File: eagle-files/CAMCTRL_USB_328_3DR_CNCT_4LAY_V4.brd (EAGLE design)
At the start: 56.6 x 37.5 mm, 71 parts, among them IC2 lm1117, J1 ICSP, Q1 12MHz, U1 M3421E, U2 ATMEGA168, U3 3.3V_REG, U4 TS3USB30EDGSR, Y1 16MHz

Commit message: Updated Code and Board
Updated test code with new object info handling, zooming command and
some extra clean-ups.
Board updated with replaced LED's resistors.
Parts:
- R13, R2, R6: value 1K -> 220R
- R14: value 330 -> 100R
- R17, R18: value 270R -> 220R
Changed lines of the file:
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@@
 </element>
 <element name="Q1" library="SparkFun-FreqCtrl" package="CRYSTAL-SMD-5X3" value="12MHz" x="11.43" y="12.065" rot="R90"/>
-<element name="R2" library="pel_dipol_comp" package="0402-RES" value="1K" x="35.56" y="8.255" rot="R90"/>
+<element name="R2" library="pel_dipol_comp" package="0402-RES" value="220R" x="35.56" y="8.255" rot="R90"/>
 <element name="C2" library="pel_dipol_comp" package="0402-CAP" value="0.1uF" x="41.91" y="6.35" rot="R270"/>
 <element name="LED1" library="pel_dipol_comp" package="0603-LED" value="GREEN" x="35.56" y="11.43" smashed="yes" rot="R270">
@@
 <attribute name="VALUE" x="37.084" y="10.3505" size="0.4064" layer="27"/>
 </element>
-<element name="R14" library="pel_dipol_comp" package="0402-RES" value="330" x="38.1" y="8.255" rot="R90"/>
+<element name="R14" library="pel_dipol_comp" package="0402-RES" value="100R" x="38.1" y="8.255" rot="R90"/>
 <element name="C10" library="SparkFun" package="EIA3216" value="10uF" x="6.985" y="3.175" rot="R270"/>
 <element name="F1" library="SparkFun" package="PTC-1206" value="PTCSMD" x="10.16" y="21.336"/>
@@
 <attribute name="VALUE" x="18.923" y="18.161" size="0.4064" layer="27" font="vector" rot="R90"/>
 </element>
-<element name="R6" library="pel_dipol_comp" package="0402-RES" value="1K" x="33.02" y="8.255" rot="R90"/>
+<element name="R6" library="pel_dipol_comp" package="0402-RES" value="220R" x="33.02" y="8.255" rot="R90"/>
 <element name="LED3" library="pel_dipol_comp" package="0603-LED" value="BLUE" x="33.02" y="11.43" smashed="yes" rot="R270">
 <attribute name="NAME" x="32.3215" y="9.271" size="0.635" layer="25" ratio="16" rot="R90"/>
@@
 <element name="SJ1" library="SparkFun-Passives" package="SJ_3_PASTE2&amp;3" value="" x="35.56" y="27.94" rot="MR180"/>
 <element name="SJ2" library="SparkFun-Passives" package="SJ_2S-NO" value="SOLDERJUMPER-OLDNO" x="38.735" y="27.94" rot="MR180"/>
-<element name="R13" library="pel_dipol_comp" package="0402-RES" value="1K" x="40.64" y="8.255" rot="R90"/>
+<element name="R13" library="pel_dipol_comp" package="0402-RES" value="220R" x="40.64" y="8.255" rot="R90"/>
 <element name="LED4" library="pel_dipol_comp" package="0603-LED" value="BLUE" x="40.64" y="11.43" smashed="yes" rot="R270">
 <attribute name="NAME" x="39.9415" y="9.271" size="0.635" layer="25" ratio="16" rot="R90"/>
@@
 <attribute name="VALUE" x="46.7614" y="26.797" size="0.635" layer="27" font="vector" ratio="16" rot="R90"/>
 </element>
-<element name="R17" library="pel_dipol_comp" package="0402-RES" value="270R" x="45.085" y="22.86" smashed="yes" rot="R270">
+<element name="R17" library="pel_dipol_comp" package="0402-RES" value="220R" x="45.085" y="22.86" smashed="yes" rot="R270">
 <attribute name="NAME" x="45.9232" y="24.003" size="0.4064" layer="25" font="vector" ratio="16" rot="R270"/>
 <attribute name="VALUE" x="43.7896" y="24.003" size="0.635" layer="27" font="vector" ratio="16" rot="R270"/>
 </element>
-<element name="R18" library="pel_dipol_comp" package="0402-RES" value="270R" x="53.975" y="17.78" smashed="yes" rot="R90">
+<element name="R18" library="pel_dipol_comp" package="0402-RES" value="220R" x="53.975" y="17.78" smashed="yes" rot="R90">
 <attribute name="NAME" x="55.0418" y="17.272" size="0.4064" layer="25" font="vector" ratio="16" rot="R90"/>
 <attribute name="VALUE" x="55.2704" y="16.637" size="0.635" layer="27" font="vector" ratio="16" rot="R90"/>
 </element>
 <element name="LED5" library="pel_dipol_comp" package="0603-LED" value="GREEN" x="50.165" y="19.05" smashed="yes" rot="R90">
-<attribute name="NAME" x="51.562" y="17.9832" size="0.4064" layer="25" font="vector" ratio="16"/>
+<attribute name="NAME" x="51.2318" y="20.447" size="0.4064" layer="25" font="vector" ratio="16" rot="R90"/>
 <attribute name="VALUE" x="51.4604" y="17.907" size="0.635" layer="27" font="vector" ratio="16" rot="R90"/>
 </element>
 <element name="LED6" library="pel_dipol_comp" package="0603-LED" value="RED" x="52.07" y="19.05" smashed="yes" rot="R90">
-<attribute name="NAME" x="53.467" y="17.9832" size="0.4064" layer="25" font="vector" ratio="16"/>
+<attribute name="NAME" x="52.5018" y="20.447" size="0.4064" layer="25" font="vector" ratio="16" rot="R90"/>
 <attribute name="VALUE" x="53.3654" y="17.907" size="0.635" layer="27" font="vector" ratio="16" rot="R90"/>
 </element>

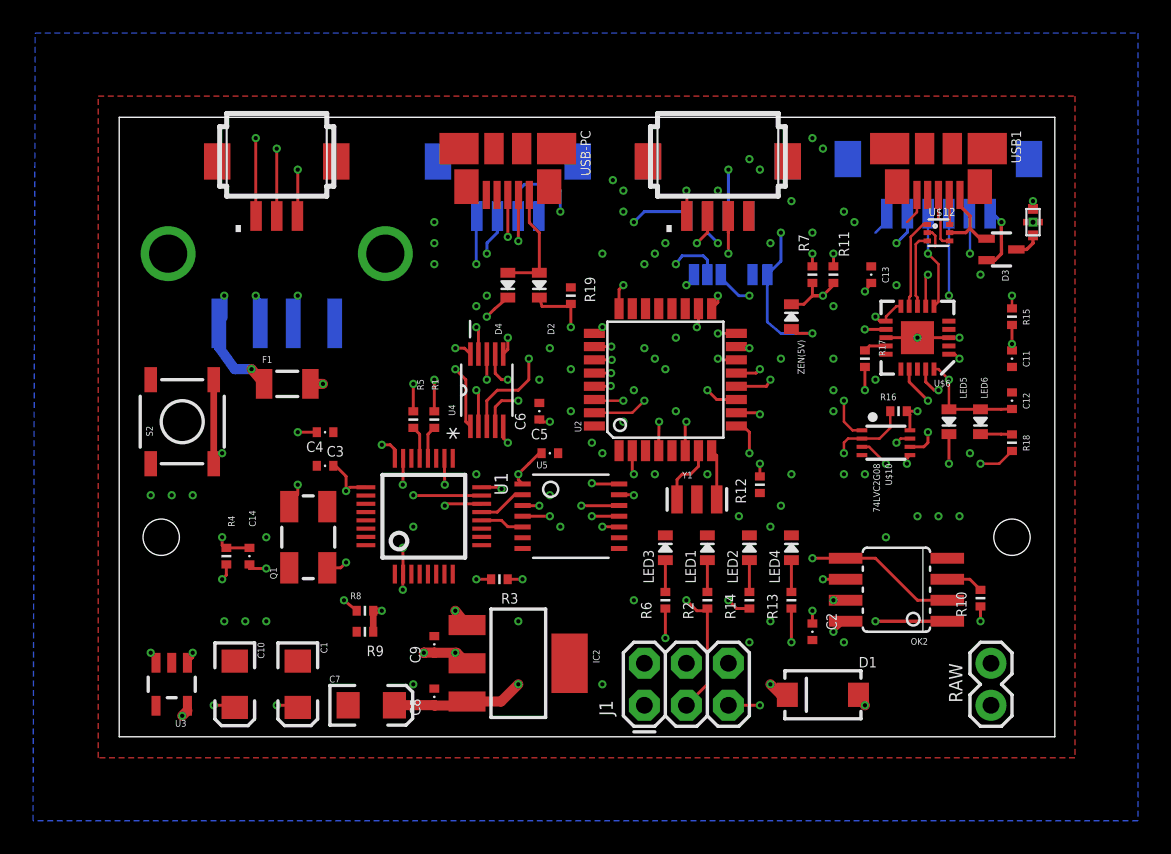
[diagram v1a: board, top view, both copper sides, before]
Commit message: Prototype V2
USB interruption line added;
VCC vs 5V wrong propagation corrected.
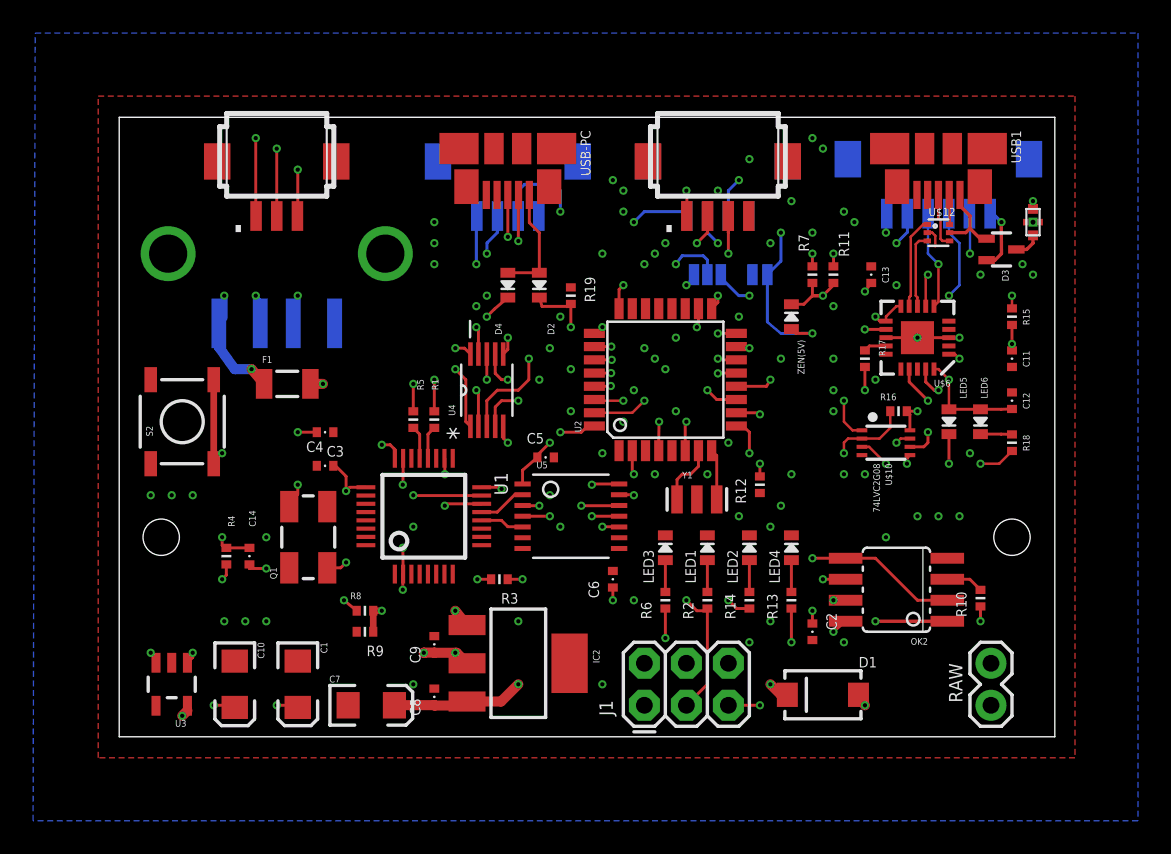
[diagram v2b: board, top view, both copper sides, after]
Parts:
- moved C6 11.1 mm to (29.8, 9.53)
- moved C5 0.36 mm to (25.8, 16.9)
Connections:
- removed net D9: DIGITAL_PINS.P$2, U2.13
- removed net N$11: R3.P$2, U1.18
- removed net VCC: C6.P$1, U4.10, U5.14
- new net INT: R3.P$2, U1.18, U2.13
- net 3.3V: now also U4.10
- net 5V: now also C6.P$1, U5.14
- net D2: now also DIGITAL_PINS.P$2
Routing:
- net INT: track 0.00 -> 33.2 mm, vias 0 -> 4
- net D2: track 0.00 -> 30.7 mm, vias 0 -> 4
- net VCC: track 19.6 -> 0.00 mm, vias 5 -> 0
- net D9: track 18.3 -> 0.00 mm, vias 3 -> 0
- net 3.3V: track 19.7 -> 32.8 mm, vias 11 -> 13
- net N$11: track 11.0 -> 0.00 mm, vias 3 -> 0
- net 5V: track 31.9 -> 35.6 mm, vias 17 -> 19
- net GND: track 11.7 -> 9.57 mm, vias 20 -> 23
- net RXD: track 40.7 -> 41.2 mm

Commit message: Prototype V2.1
4k7 resistor added to the USB-Mux's "select" pin.
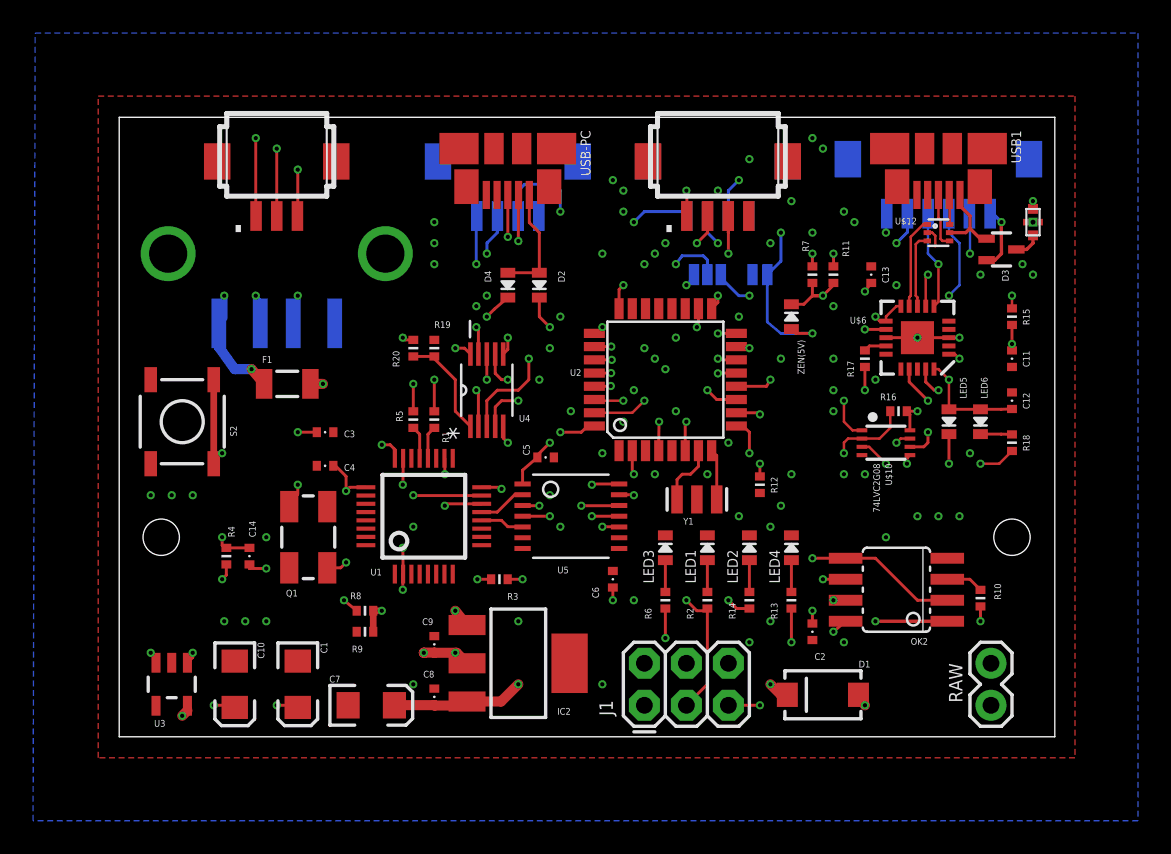
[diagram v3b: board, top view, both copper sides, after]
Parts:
- added R20: 4K7, pel_dipol_comp:0402-RES
- moved R19 8.84 mm to (19.1, 23.5)
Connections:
- new net N$28: D2.C, R20.P$2
- net PC_SEL: now also R20.P$1; no longer D2.C
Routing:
- net N$28: track 0.00 -> 11.9 mm, vias 0 -> 2
- net PC_SEL: track 17.1 -> 6.40 mm, vias 3 -> 0

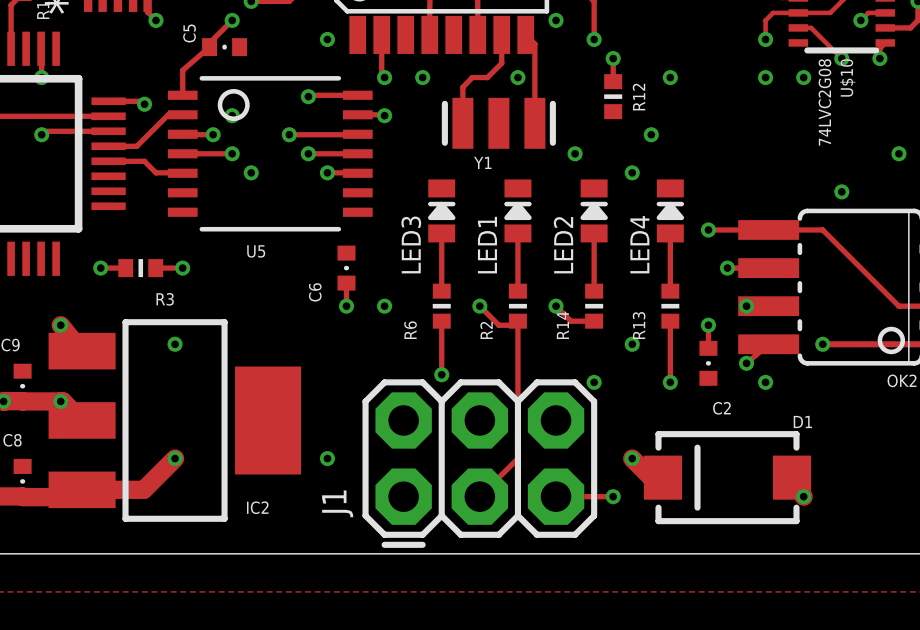
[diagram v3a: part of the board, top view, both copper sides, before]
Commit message: Level Converter Replacement
TXB0104PWR replaced by a TXS0104PWR (larger current draw on the IO). A
10K OE resistor was added as well.
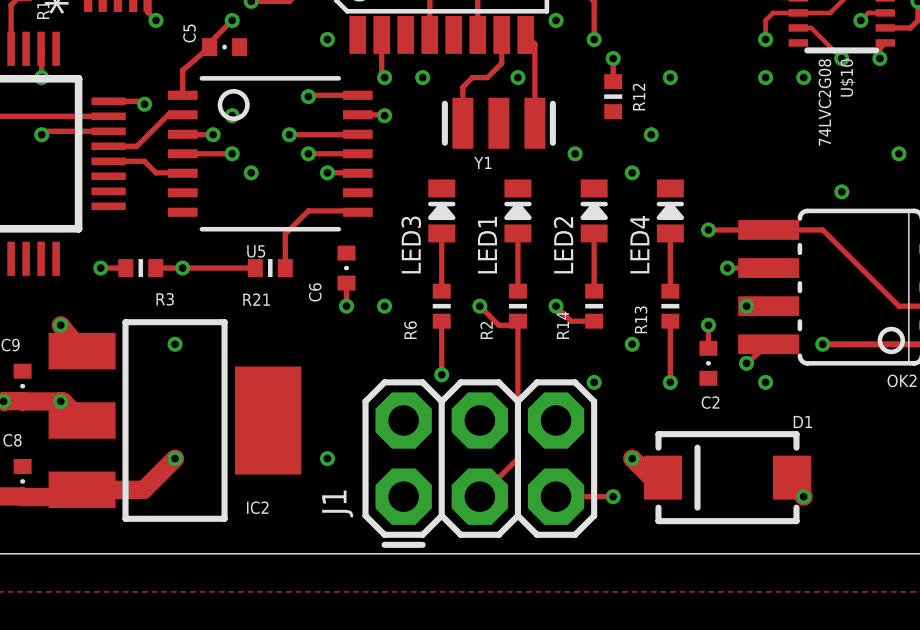
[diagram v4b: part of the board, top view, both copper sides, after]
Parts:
- added R21: 10K, pel_dipol_comp:0402-RES
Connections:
- new net N$29: R21.P$2, U5.8
- net 3.3V: now also R21.P$1
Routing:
- net N$29: track 0.00 -> 3.89 mm
- net 3.3V: track 32.8 -> 35.2 mm
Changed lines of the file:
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@@
 </element>
 <element name="C2" library="pel_dipol_comp" package="0402-CAP" value="0.1uF" x="41.91" y="6.35" smashed="yes" rot="R270">
-<attribute name="NAME" x="42.037" y="4.6482" size="0.4064" layer="25" font="vector" ratio="16"/>
+<attribute name="NAME" x="41.656" y="4.8387" size="0.4064" layer="25" font="vector" ratio="16"/>
 <attribute name="VALUE" x="40.6146" y="7.493" size="0.635" layer="27" font="vector" ratio="16" rot="R270"/>
 </element>
@@
 </element>
 <element name="R13" library="pel_dipol_comp" package="0402-RES" value="220R" x="40.64" y="8.255" smashed="yes" rot="R90">
-<attribute name="NAME" x="39.8018" y="7.112" size="0.4064" layer="25" font="vector" ratio="16" rot="R90"/>
+<attribute name="NAME" x="39.8653" y="7.3025" size="0.4064" layer="25" font="vector" ratio="16" rot="R90"/>
 <attribute name="VALUE" x="41.9354" y="7.112" size="0.635" layer="27" font="vector" ratio="16" rot="R90"/>
 </element>
@@
 <attribute name="NAME" x="16.9418" y="22.352" size="0.4064" layer="25" font="vector" ratio="16" rot="R90"/>
 <attribute name="VALUE" x="19.0754" y="22.352" size="0.635" layer="27" font="vector" ratio="16" rot="R90"/>
+</element>
+<element name="R21" library="pel_dipol_comp" package="0402-RES" value="10K" x="27.305" y="9.525" smashed="yes">
+<attribute name="NAME" x="26.3525" y="8.2677" size="0.4064" layer="25" font="vector" ratio="16"/>
+<attribute name="VALUE" x="26.162" y="8.2296" size="0.635" layer="27" font="vector" ratio="16"/>
 </element>
 </elements>
@@
 <wire x1="48.23" y1="32.76" x2="48.855" y2="30.48" width="0" layer="19" extent="1-1"/>
 </signal>
-<signal name="5V">
+<signal name="5V" airwireshidden="yes">
 <contactref element="C2" pad="P$1"/>
 <contactref element="J1" pad="2"/>
@@
 <wire x1="7.724" y1="11.422" x2="7.874" y2="11.422" width="0.1778" layer="1"/>
 </signal>
-<signal name="3.3V">
+<signal name="3.3V" airwireshidden="yes">
 <contactref element="U1" pad="23"/>
 <contactref element="U1" pad="2"/>
@@
 <wire x1="20.32" y1="23.495" x2="20.8788" y2="23.495" width="0.1778" layer="1"/>
 <wire x1="20.8788" y1="23.495" x2="21.2344" y2="23.1394" width="0.1778" layer="1"/>
+<contactref element="R21" pad="P$1"/>
+<wire x1="26.805" y1="9.525" x2="24.384" y2="9.525" width="0.1778" layer="1"/>
 </signal>
 <signal name="N$5">
@@
 <wire x1="25.4" y1="25.4" x2="25.4" y2="26.555" width="0.1778" layer="1"/>
 </signal>
+<signal name="N$29">
+<contactref element="U5" pad="8"/>
+<contactref element="R21" pad="P$2"/>
+<wire x1="27.805" y1="9.525" x2="27.805" y2="10.66" width="0.1778" layer="1"/>
+<wire x1="27.805" y1="10.66" x2="28.575" y2="11.43" width="0.1778" layer="1"/>
+<wire x1="28.575" y1="11.43" x2="30.1778" y2="11.43" width="0.1778" layer="1"/>
+<wire x1="30.1778" y1="11.43" x2="30.2228" y2="11.385" width="0.1778" layer="1"/>
+</signal>
 </signals>
